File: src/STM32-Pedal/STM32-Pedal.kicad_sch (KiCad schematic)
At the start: 0 parts

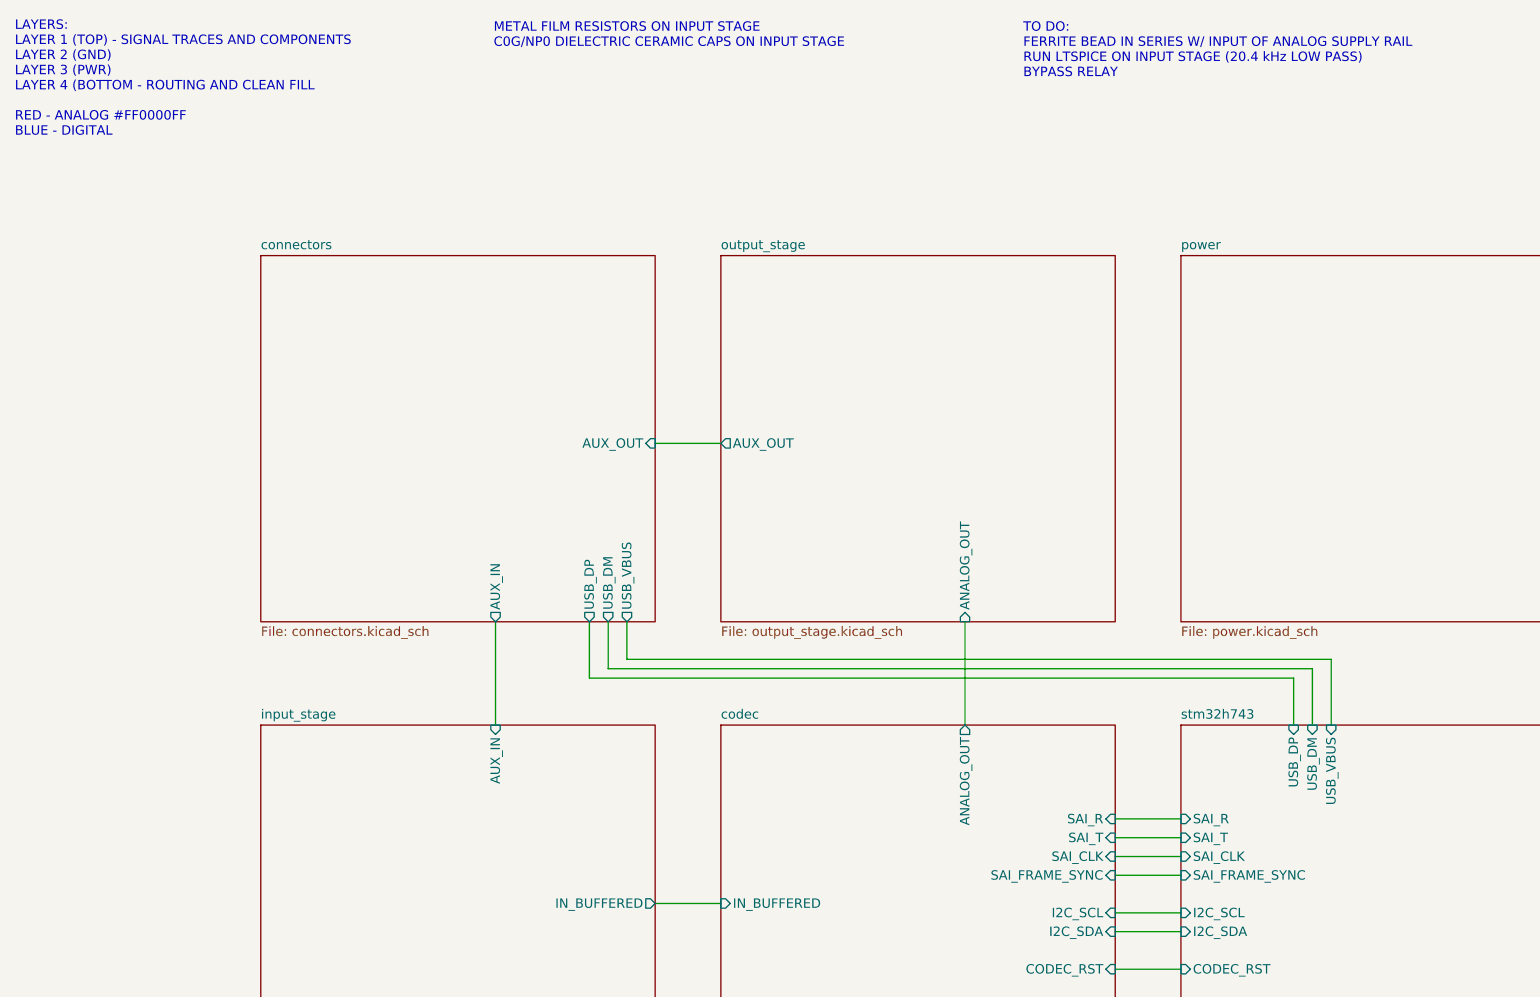
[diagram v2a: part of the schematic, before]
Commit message: Schematic: bypass relay, cleaning up input stage
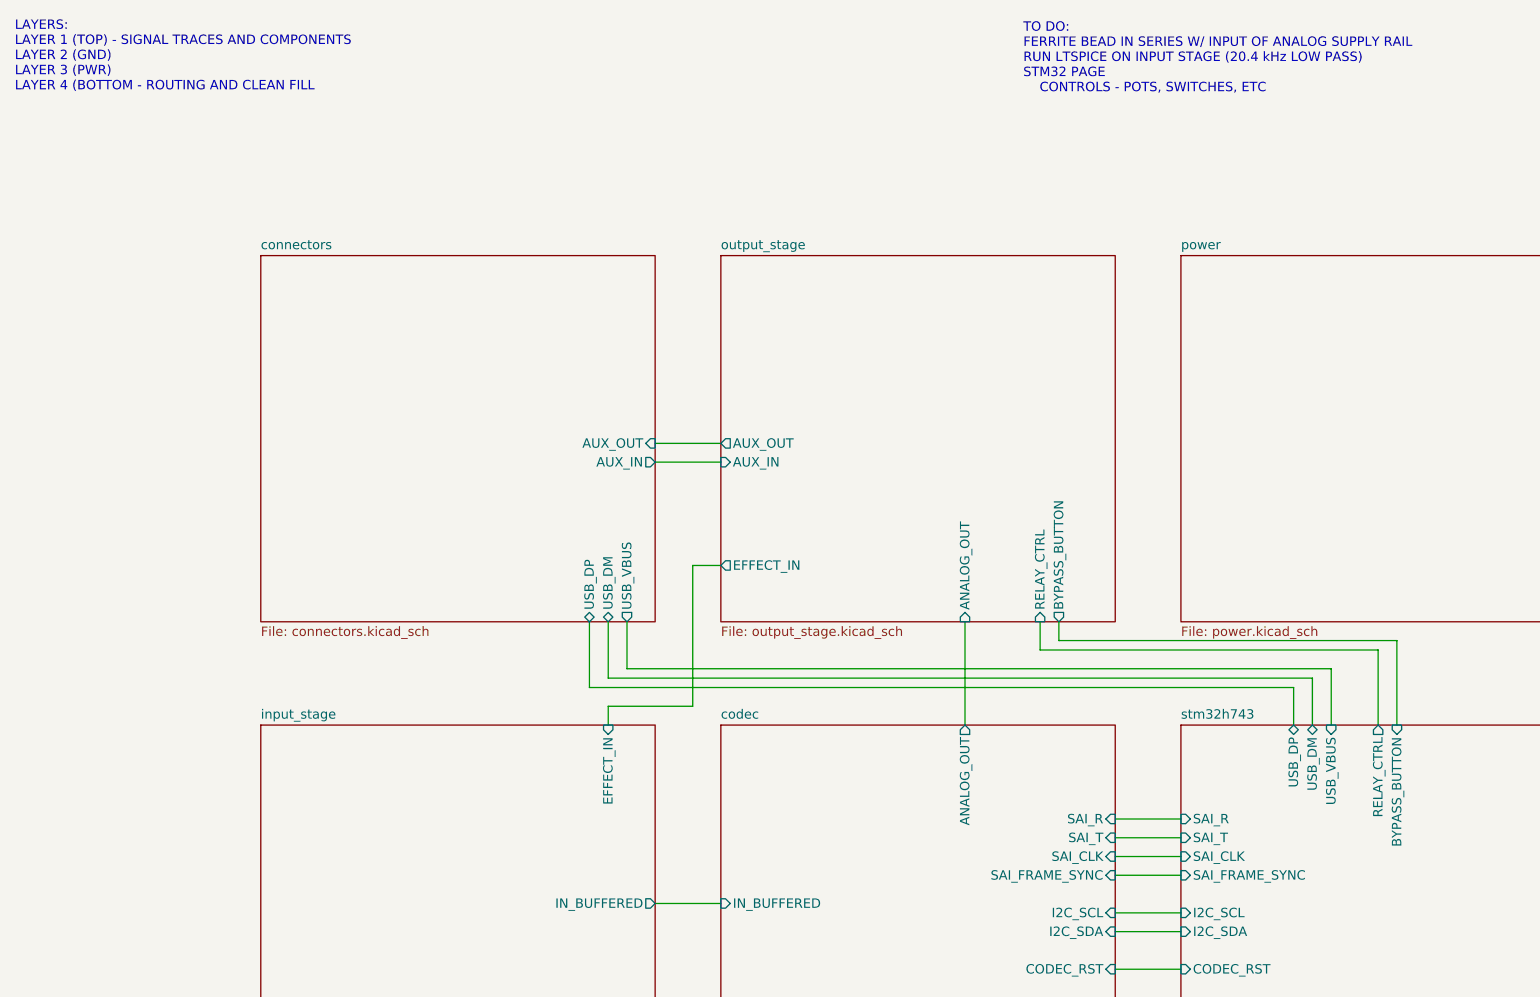
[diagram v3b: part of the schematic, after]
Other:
- sheet input_stage ports: added EFFECT_IN; removed AUX_IN
- sheet output_stage ports: added AUX_IN, BYPASS_BUTTON, EFFECT_IN, RELAY_CTRL; removed none
- sheet stm32h743 ports: added BYPASS_BUTTON, RELAY_CTRL; removed none
- note added: "LAYERS: LAYER 1 (TOP) - SIGNAL TRACES AND COMPONENTS LAYER 2 (GND) LAYER 3 (PWR) LAYER 4 (BOTTOM - ROUTING AND CLEAN FILL"
- note added: "TO DO: FERRITE BEAD IN SERIES W/ INPUT OF ANALOG SUPPLY RAIL RUN LTSPICE ON INPUT STAGE (20.4 kHz LOW PASS) STM32 PAGE CONTROLS - POTS, SWITCHES, ETC"
- note removed: "LAYERS: LAYER 1 (TOP) - SIGNAL TRACES AND COMPONENTS LAYER 2 (GND) LAYER 3 (PWR) LAYER 4 (BOTTOM - ROUTING AND CLEAN FILL RED - ANALOG #FF0000FF BLUE - DIGITAL"
- note removed: "METAL FILM RESISTORS ON INPUT STAGE C0G/NP0 DIELECTRIC CERAMIC CAPS ON INPUT STAGE"
- note removed: "TO DO: FERRITE BEAD IN SERIES W/ INPUT OF ANALOG SUPPLY RAIL RUN LTSPICE ON INPUT STAGE (20.4 kHz LOW PASS) BYPASS RELAY"
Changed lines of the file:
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@@
 	(generator_version "10.0")
 	(paper "USLetter")
-	(text "METAL FILM RESISTORS ON INPUT STAGE\nC0G/NP0 DIELECTRIC CERAMIC CAPS ON INPUT STAGE"
-		(exclude_from_sim no)
-		(at 82.296 19.304 0)
-		(effects
-			(font
-				(size 1.27 1.27)
-			)
-			(justify left top)
-		)
-	)
 	(text "PCB LAYOUT NOTES:\nUSB Differentials - target 90 ohms differential impedance"
 		(exclude_from_sim no)
@@
 		)
 	)
-	(text "TO DO:\nFERRITE BEAD IN SERIES W/ INPUT OF ANALOG SUPPLY RAIL\nRUN LTSPICE ON INPUT STAGE (20.4 kHz LOW PASS)\nBYPASS RELAY"
+	(text "TO DO:\nFERRITE BEAD IN SERIES W/ INPUT OF ANALOG SUPPLY RAIL\nRUN LTSPICE ON INPUT STAGE (20.4 kHz LOW PASS)\nSTM32 PAGE\n	CONTROLS - POTS, SWITCHES, ETC"
 		(exclude_from_sim no)
 		(at 153.924 19.304 0)
@@
 		)
 	)
-	(text "LAYERS:\nLAYER 1 (TOP) - SIGNAL TRACES AND COMPONENTS\nLAYER 2 (GND)\nLAYER 3 (PWR)\nLAYER 4 (BOTTOM - ROUTING AND CLEAN FILL\n\nRED - ANALOG #FF0000FF\nBLUE - DIGITAL"
+	(text "LAYERS:\nLAYER 1 (TOP) - SIGNAL TRACES AND COMPONENTS\nLAYER 2 (GND)\nLAYER 3 (PWR)\nLAYER 4 (BOTTOM - ROUTING AND CLEAN FILL"
 		(exclude_from_sim no)
 		(at 17.526 19.05 0)
@@
 	(wire
 		(pts
-			(xy 100.33 105.41) (xy 195.58 105.41)
+			(xy 113.03 92.71) (xy 109.22 92.71)
+		)
+		(stroke
+			(width 0)
+			(type default)
+		)
+	)
+	(wire
+		(pts
+			(xy 109.22 111.76) (xy 97.79 111.76)
+		)
+		(stroke
+			(width 0)
+			(type default)
+		)
+	)
+	(wire
+		(pts
+			(xy 104.14 78.74) (xy 113.03 78.74)
+		)
+		(stroke
+			(width 0)
+			(type default)
+		)
+	)
+	(wire
+		(pts
+			(xy 156.21 104.14) (xy 156.21 100.33)
+		)
+		(stroke
+			(width 0)
+			(type default)
+		)
+	)
+	(wire
+		(pts
+			(xy 100.33 106.68) (xy 195.58 106.68)
 		)
 		(stroke
@@
 	(wire
 		(pts
-			(xy 193.04 106.68) (xy 193.04 114.3)
+			(xy 204.47 114.3) (xy 204.47 102.87)
+		)
+		(stroke
+			(width 0)
+			(type default)
+		)
+	)
+	(wire
+		(pts
+			(xy 158.75 100.33) (xy 158.75 102.87)
+		)
+		(stroke
+			(width 0)
+			(type default)
+		)
+	)
+	(wire
+		(pts
+			(xy 193.04 107.95) (xy 193.04 114.3)
 		)
 		(stroke
@@
 	(wire
 		(pts
-			(xy 95.25 107.95) (xy 190.5 107.95)
-		)
-		(stroke
-			(width 0)
-			(type default)
-		)
-	)
-	(wire
-		(pts
-			(xy 195.58 105.41) (xy 195.58 114.3)
+			(xy 95.25 109.22) (xy 190.5 109.22)
+		)
+		(stroke
+			(width 0)
+			(type default)
+		)
+	)
+	(wire
+		(pts
+			(xy 201.93 114.3) (xy 201.93 104.14)
+		)
+		(stroke
+			(width 0)
+			(type default)
+		)
+	)
+	(wire
+		(pts
+			(xy 195.58 106.68) (xy 195.58 114.3)
+		)
+		(stroke
+			(width 0)
+			(type default)
+		)
+	)
+	(wire
+		(pts
+			(xy 97.79 111.76) (xy 97.79 114.3)
 		)
 		(stroke
@@
 	(wire
 		(pts
-			(xy 190.5 107.95) (xy 190.5 114.3)
-		)
-		(stroke
-			(width 0)
-			(type default)
-		)
-	)
-	(wire
-		(pts
-			(xy 100.33 100.33) (xy 100.33 105.41)
+			(xy 190.5 109.22) (xy 190.5 114.3)
+		)
+		(stroke
+			(width 0)
+			(type default)
+		)
+	)
+	(wire
+		(pts
+			(xy 100.33 100.33) (xy 100.33 106.68)
 		)
 		(stroke
@@
 	(wire
 		(pts
-			(xy 95.25 100.33) (xy 95.25 107.95)
-		)
-		(stroke
-			(width 0)
-			(type default)
-		)
-	)
-	(wire
-		(pts
-			(xy 82.55 100.33) (xy 82.55 114.3)
-		)
-		(stroke
-			(width 0)
-			(type default)
-		)
-	)
-	(wire
-		(pts
-			(xy 97.79 106.68) (xy 193.04 106.68)
-		)
-		(stroke
-			(width 0)
-			(type default)
-		)
-	)
-	(wire
-		(pts
-			(xy 97.79 100.33) (xy 97.79 106.68)
+			(xy 201.93 104.14) (xy 156.21 104.14)
+		)
+		(stroke
+			(width 0)
+			(type default)
+		)
+	)
+	(wire
+		(pts
+			(xy 95.25 100.33) (xy 95.25 109.22)
+		)
+		(stroke
+			(width 0)
+			(type default)
+		)
+	)
+	(wire
+		(pts
+			(xy 97.79 107.95) (xy 193.04 107.95)
+		)
+		(stroke
+			(width 0)
+			(type default)
+		)
+	)
+	(wire
+		(pts
+			(xy 97.79 100.33) (xy 97.79 107.95)
+		)
+		(stroke
+			(width 0)
+			(type default)
+		)
+	)
+	(wire
+		(pts
+			(xy 109.22 92.71) (xy 109.22 111.76)
+		)
+		(stroke
+			(width 0)
+			(type default)
+		)
+	)
+	(wire
+		(pts
+			(xy 204.47 102.87) (xy 158.75 102.87)
 		)
 		(stroke
@@
 			)
 		)
-		(pin "AUX_IN" input
-			(at 82.55 114.3 90)
+		(pin "EFFECT_IN" input
+			(at 97.79 114.3 90)
 			(effects
 				(font
@@
 		)
 		(pin "AUX_IN" output
-			(at 82.55 100.33 270)
-			(effects
-				(font
-					(size 1.27 1.27)
-				)
-				(justify left)
+			(at 104.14 78.74 0)
+			(effects
+				(font
+					(size 1.27 1.27)
+				)
+				(justify right)
 			)
 		)
@@
 			)
 		)
-		(pin "USB_DM" output
+		(pin "USB_DM" bidirectional
 			(at 97.79 100.33 270)
 			(effects
@@
 			)
 		)
-		(pin "USB_DP" output
+		(pin "USB_DP" bidirectional
 			(at 95.25 100.33 270)
 			(effects
@@
 			)
 		)
+		(pin "AUX_IN" input
+			(at 113.03 78.74 180)
+			(effects
+				(font
+					(size 1.27 1.27)
+				)
+				(justify left)
+			)
+		)
+		(pin "RELAY_CTRL" input
+			(at 156.21 100.33 270)
+			(effects
+				(font
+					(size 1.27 1.27)
+				)
+				(justify left)
+			)
+		)
+		(pin "EFFECT_IN" output
+			(at 113.03 92.71 180)
+			(effects
+				(font
+					(size 1.27 1.27)
+				)
+				(justify left)
+			)
+		)
+		(pin "BYPASS_BUTTON" output
+			(at 158.75 100.33 270)
+			(effects
+				(font
+					(size 1.27 1.27)
+				)
+				(justify left)
+			)
+		)
 		(instances
 			(project "STM32-Pedal"
@@
 			)
 		)
-		(pin "USB_DM" input
+		(pin "USB_DM" bidirectional
 			(at 193.04 114.3 90)
 			(effects
@@
 			)
 		)
-		(pin "USB_DP" input
+		(pin "USB_DP" bidirectional
 			(at 190.5 114.3 90)
 			(effects
@@
 			(effects
 				(font
+					(size 1.27 1.27)
+				)
+				(justify right)
+			)
+		)
+		(pin "BYPASS_BUTTON" input
+			(at 204.47 114.3 90)
+			(effects
+				(font
+					(size 1.27 1.27)
+				)
+				(justify right)
+			)
+		)
+		(pin "RELAY_CTRL" output
+			(at 201.93 114.3 90)
+			(effects
+				(font
